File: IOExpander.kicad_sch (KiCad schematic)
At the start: 2 parts, among them U12 PCA9536D

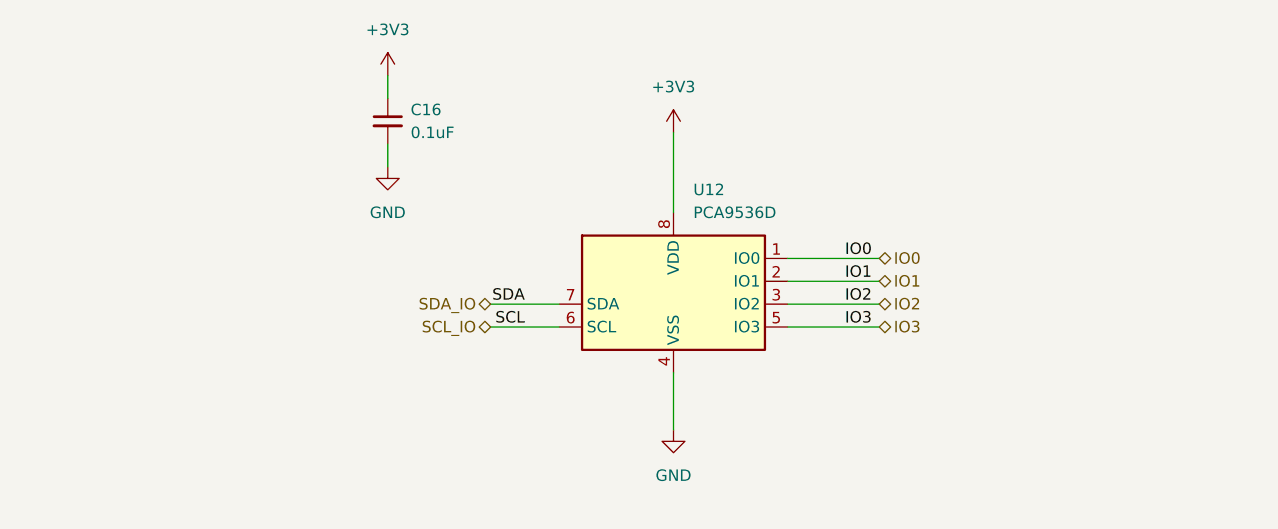
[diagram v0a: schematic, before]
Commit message: Refactored schematics and silkscreen
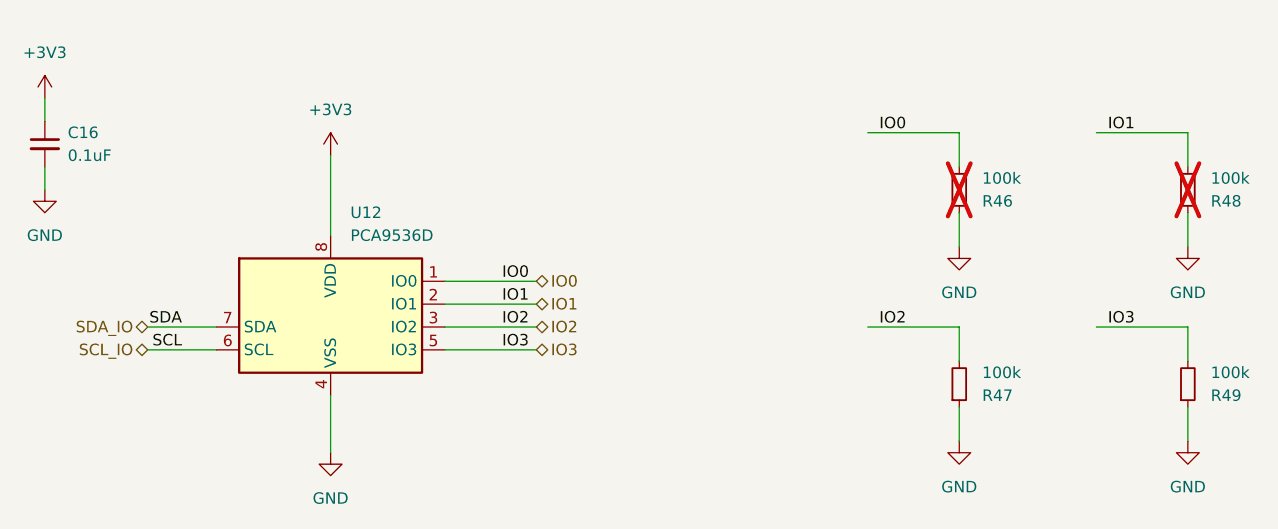
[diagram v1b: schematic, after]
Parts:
- added R46, R48: 100k, Resistor_SMD:R_0603_1608Metric, symbol Device:R_Small
- added R47, R49: 100k, Capacitor_SMD:C_0603_1608Metric, symbol Device:R_Small
- C16: footprint (none) -> Capacitor_SMD:C_0603_1608Metric
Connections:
- net GND: now also R46.1, R47.1, R48.1, R49.1
- net IO0: now also R46.2
- net IO1: now also R48.2
- net IO2: now also R47.2
- net IO3: now also R49.2
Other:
- moved on the sheet: C16, U12

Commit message: v2.1 (v3?) Partial Updates
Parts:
- removed R46, R48: 100k, Resistor_SMD:R_0603_1608Metric, symbol Device:R_Small
- removed R47, R49: 100k, Capacitor_SMD:C_0603_1608Metric, symbol Device:R_Small
- removed U12: PCA9536D, Package_SO:SOIC-8_3.9x4.9mm_P1.27mm, symbol Interface_Expansion:PCA9536D
- added F9: 1A, Fuse:Fuse_0805_2012Metric, symbol Device:Polyfuse_Small
- added R73, R74, R75, R76, R77, R78, R79: 10k, Resistor_SMD:R_0603_1608Metric, symbol Device:R_Small
- added U7: MAX7310, Package_DFN_QFN:QFN-16-1EP_4x4mm_P0.65mm_EP2.1x2.1mm, symbol Argus-IC:MAX7310
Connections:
- net +3V3: now also F9.2; no longer C16.1
- net GND: now also R74.2, R76.2, R78.2, U7.17 (GND), U7.6 (GND), U7.EPAD (GND)
- net IO0: now also U7.4 (IO0)
- net IO1: now also U7.5 (IO1)
- net IO2: now also U7.7 (IO2)
- net IO3: now also U7.8 (IO3)
- new net: C16.1, F9.1, R73.1, R75.1, R77.1, R79.2, U7.14 (V+)
- new net: R79.1, U7.13 (~{RESET})
- new net AD0: R73.2, R74.1, U7.1 (AD0)
- new net AD1: R75.2, R76.1, U7.2 (AD1)
- new net AD2: R77.2, R78.1, U7.3 (AD2)
- new net IO4: U7.9 (IO4)
- new net IO5: U7.10 (IO5)
- new net IO6: U7.11 (IO6)
- new net IO7: U7.12 (IO7)
- new net SCL: U7.15 (SCL)
- new net SDA: U7.16 (SDA)
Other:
- added sheet I2C Protection1 (I2CProtection.kicad_sch)
- note added: "REPLACE FUSE WITH LOAD SWITCH?"
- company: (none) -> Carnegie Mellon University
- title: (none) -> Argus Batteryboard
- moved on the sheet: C16
